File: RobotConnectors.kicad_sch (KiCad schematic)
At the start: 87 parts, among them J1 Conn_02x11_Top_Bottom, J10 Conn_01x05, J11 SA/SC Perimeter Plug, J12 Conn_01x03_Pin, J13 Conn_01x03_Pin, J14 Conn_01x03_Pin, J15 Conn_01x03_Pin, J17 Conn_01x02, J18 Conn_01x02, J19 Conn_01x04, J2 Conn_02x04_Top_Bottom, J21 Conn_01x05, J27 Conn_01x02_Pin, J3 Conn_01x02, J4 Conn_01x04, J40 Conn_01x02_Pin, J5 OEM CoverUI, J6 Conn_01x14_Socket, J7 Conn_01x12_Socket, J8 Conn_01x03_Pin, J9 Conn_01x03_Pin, U11 SN74LVC07ADBR, U12 SN74LVC07ADBR, U14 Fuse Holder, U15 Fuse Holder, U16 Fuse Holder, U17 Fuse Holder, U2 TPS2065CDBV, U28 Fuse 2A, U29 Fuse 2A, U47 SN74LVC157ADR, U48 SN74LVC157ADR

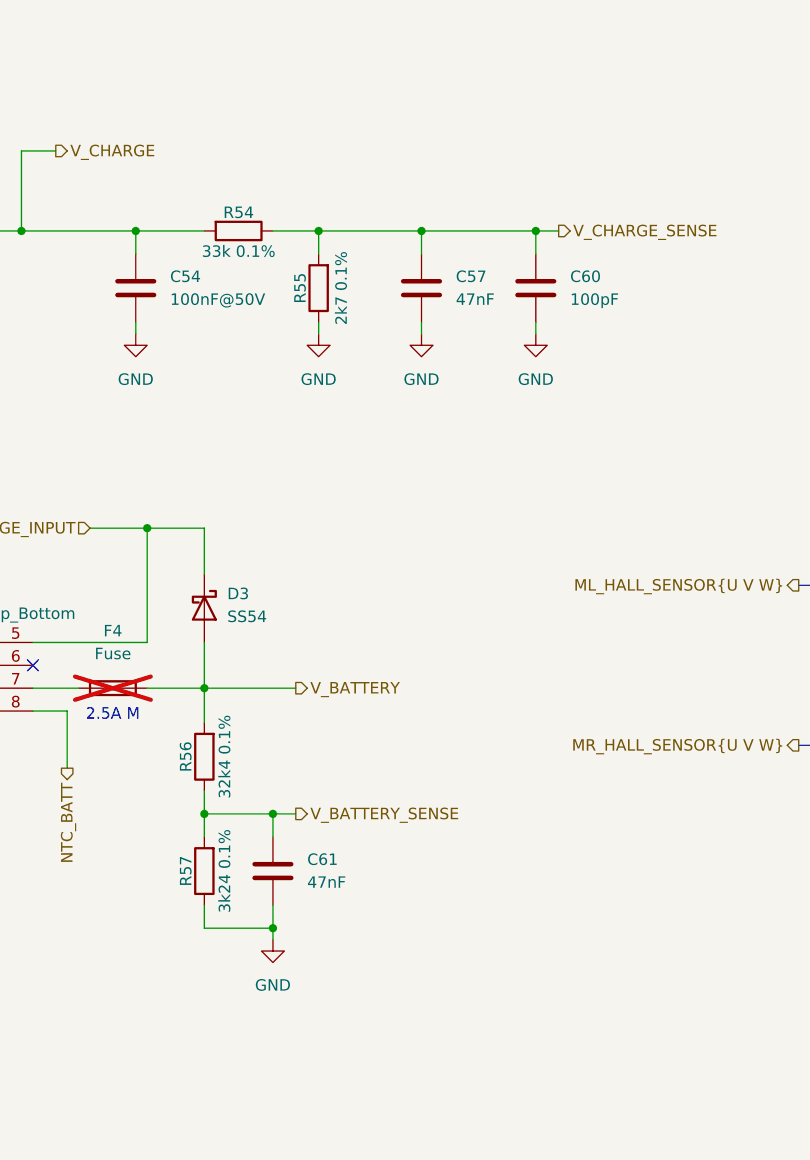
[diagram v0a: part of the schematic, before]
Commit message: Added filter to VBATT and VCHARGE rails, increased cap to 470nF, moved cap close to xCore (fixes #14)
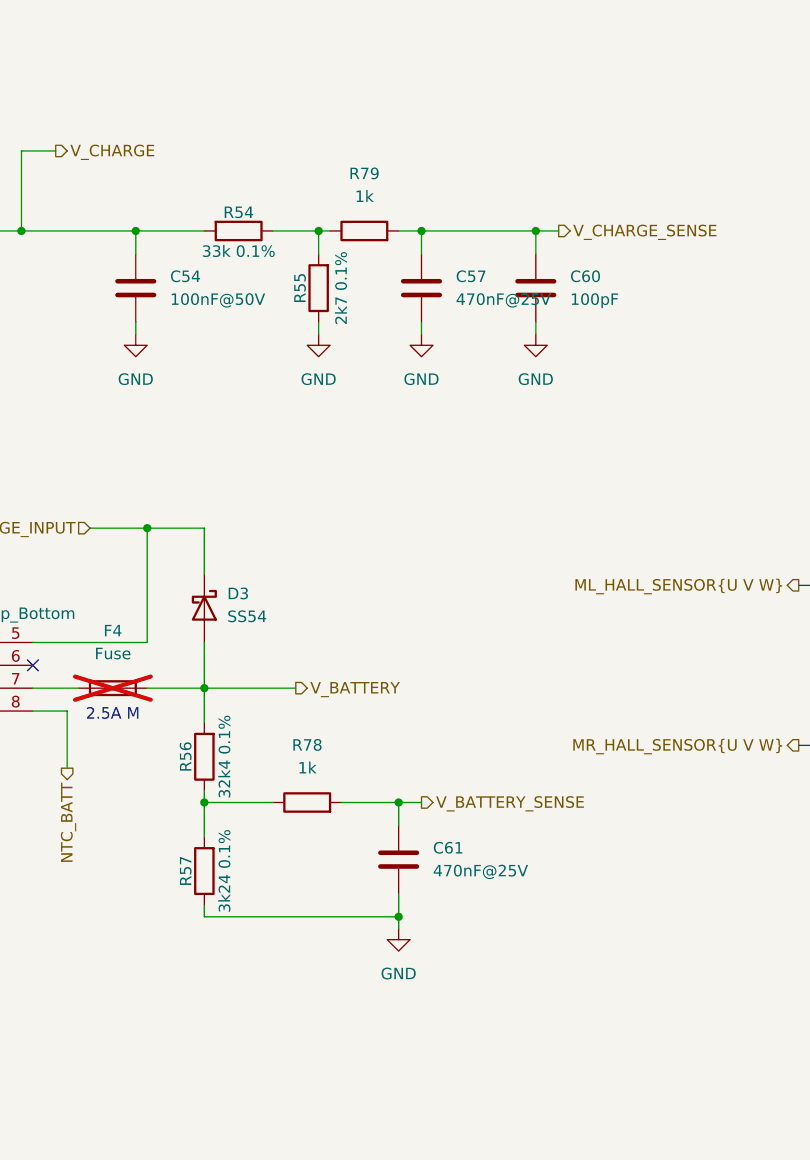
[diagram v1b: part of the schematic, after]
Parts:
- added R78, R79: 1k, Resistor_SMD:R_0603_1608Metric, symbol Device:R
- C57, C61: value 47nF -> 470nF@25V; JLC C1622 -> C1623
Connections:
- net V_BATTERY_SENSE: now also R78.2; no longer R56.1, R57.2
- net V_CHARGE_SENSE: now also R79.2; no longer R54.1, R55.2
- new net: R56.1, R57.2, R78.1
- new net: R54.1, R55.2, R79.1
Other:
- moved on the sheet: C61
